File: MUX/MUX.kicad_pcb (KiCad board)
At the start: 4 copper layers, 364 x 203 mm, 100 parts, among them P1 Conn_02x36_Top_Bottom, P2 DB9_Male, P3 DB9_Male, P4 DB9_Male, P5 DB9_Male

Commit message: MUX: Start of the layout
Let's see how it goes...
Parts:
- moved R16 24.6 mm to (290.8, 170.6)
- moved R15 4.19 mm to (321.3, 55.5)
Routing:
- net /~{Reset}: track 0.00 -> 268.7 mm, vias 0 -> 1
- net /Reset: track 0.00 -> 263.3 mm
- net /~{INT_Request}: track 0.00 -> 230.4 mm, vias 0 -> 1
- net /~{CommonAddressed}: track 0.00 -> 194.2 mm, vias 0 -> 2
- net /Data.InBD_{5}: track 0.00 -> 178.2 mm
- net /Data.InBD_{6}: track 0.00 -> 176.9 mm
- net /CausePending: track 0.00 -> 170.7 mm
- net /~{INT_INH}: track 0.00 -> 167.5 mm, vias 0 -> 1
- net /MUXClock: track 0.00 -> 159.4 mm
- net /LevelAllow: track 0.00 -> 154.9 mm
- net /INT_Request: track 0.00 -> 144.2 mm
- net Net-(U_A4-Pad1): track 0.00 -> 134.5 mm, vias 0 -> 1
- net Net-(R_C4RN1-Pad1): track 0.00 -> 128.3 mm
- net Net-(R_C4RN1-Pad2): track 0.00 -> 122.7 mm
- net Net-(R_C4RN1-Pad3): track 0.00 -> 121.7 mm
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
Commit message: MUX: Place capacitors and some power layout
Place decoupling capacitors and do some power layout to try it out
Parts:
- added C1: 100nF, Capacitor_THT:C_Disc_D4.3mm_W1.9mm_P5.00mm, F.Cu at (80.4, 46.6)
- added C10: 1000uF, Capacitor_THT:CP_Radial_D8.0mm_P3.50mm, F.Cu at (174.9, 215.9)
- added C11: 100nF, Capacitor_THT:C_Disc_D4.3mm_W1.9mm_P5.00mm, F.Cu at (209.4, 46.4)
- added C12: 100nF, Capacitor_THT:C_Disc_D4.3mm_W1.9mm_P5.00mm, F.Cu at (209.0, 69.4)
- added C13: 100nF, Capacitor_THT:C_Disc_D4.3mm_W1.9mm_P5.00mm, F.Cu at (208.8, 92.5)
- added C14: 100nF, Capacitor_THT:C_Disc_D4.3mm_W1.9mm_P5.00mm, F.Cu at (206.4, 116.3)
- added C15: 100nF, Capacitor_THT:C_Disc_D4.3mm_W1.9mm_P5.00mm, F.Cu at (208.3, 139.3)
- added C16: 100nF, Capacitor_THT:C_Disc_D4.3mm_W1.9mm_P5.00mm, F.Cu at (209.7, 162.6)
- added C17: 100nF, Capacitor_THT:C_Disc_D4.3mm_W1.9mm_P5.00mm, F.Cu at (209.4, 186.8)
- added C18: 100nF, Capacitor_THT:C_Disc_D4.3mm_W1.9mm_P5.00mm, F.Cu at (209.4, 209.9)
- added C2: 100nF, Capacitor_THT:C_Disc_D4.3mm_W1.9mm_P5.00mm, F.Cu at (80.0, 69.8)
- added C20: 1000uF, Capacitor_THT:CP_Radial_D8.0mm_P3.50mm, F.Cu at (364.6, 40.6)
- added C21: 100nF, Capacitor_THT:C_Disc_D4.3mm_W1.9mm_P5.00mm, F.Cu at (334.0, 46.9)
- added C22: 100nF, Capacitor_THT:C_Disc_D4.3mm_W1.9mm_P5.00mm, F.Cu at (334.0, 70.2)
- added C23: 100nF, Capacitor_THT:C_Disc_D4.3mm_W1.9mm_P5.00mm, F.Cu at (335.0, 93.3)
- added C24: 100nF, Capacitor_THT:C_Disc_D4.3mm_W1.9mm_P5.00mm, F.Cu at (332.2, 116.8)
- added C25: 100nF, Capacitor_THT:C_Disc_D4.3mm_W1.9mm_P5.00mm, F.Cu at (334.0, 139.8)
- added C26: 100nF, Capacitor_THT:C_Disc_D4.3mm_W1.9mm_P5.00mm, F.Cu at (332.6, 163.8)
- added C27: 100nF, Capacitor_THT:C_Disc_D4.3mm_W1.9mm_P5.00mm, F.Cu at (332.6, 186.3)
- added C28: 100nF, Capacitor_THT:C_Disc_D4.3mm_W1.9mm_P5.00mm, F.Cu at (333.9, 209.5)
- added C29: 1000uF, Capacitor_THT:CP_Radial_D8.0mm_P3.50mm, F.Cu at (364.6, 208.7)
- added C3: 100nF, Capacitor_THT:C_Disc_D4.3mm_W1.9mm_P5.00mm, F.Cu at (80.0, 88.4)
- added C31: 100nF, Capacitor_THT:C_Disc_D4.3mm_W1.9mm_P5.00mm, F.Cu at (64.8, 215.2)
- added C32: 100nF, Capacitor_THT:C_Disc_D4.3mm_W1.9mm_P5.00mm, F.Cu at (113.0, 186.3)
- added C33: 100nF, Capacitor_THT:C_Disc_D4.3mm_W1.9mm_P5.00mm, F.Cu at (176.5, 47.2)
- added C34: 100nF, Capacitor_THT:C_Disc_D4.3mm_W1.9mm_P5.00mm, F.Cu at (176.5, 116.5)
- added C35: 100nF, Capacitor_THT:C_Disc_D4.3mm_W1.9mm_P5.00mm, F.Cu at (40.0, 126.4)
- added C36: 100nF, Capacitor_THT:C_Disc_D4.3mm_W1.9mm_P5.00mm, F.Cu at (38.6, 163.4)
- added C4: 100nF, Capacitor_THT:C_Disc_D4.3mm_W1.9mm_P5.00mm, F.Cu at (80.3, 116.3)
- added C5: 100nF, Capacitor_THT:C_Disc_D4.3mm_W1.9mm_P5.00mm, F.Cu at (80.1, 139.5)
- added C6: 100nF, Capacitor_THT:C_Disc_D4.3mm_W1.9mm_P5.00mm, F.Cu at (79.9, 163.2)
- added C7: 100nF, Capacitor_THT:C_Disc_D4.3mm_W1.9mm_P5.00mm, F.Cu at (80.1, 186.1)
- added C8: 1000uF, Capacitor_THT:CP_Radial_D8.0mm_P3.50mm, F.Cu at (98.8, 33.4)
- added C9: 100nF, Capacitor_THT:C_Disc_D4.3mm_W1.9mm_P5.00mm, F.Cu at (113.0, 209.5)
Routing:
- net GND: track 41.7 -> 883.2 mm
- net +5V: track 100.3 -> 683.3 mm, vias 0 -> 1
- net +12V: track 0.00 -> 315.2 mm, vias 0 -> 1
- net -12V: track 0.00 -> 253.2 mm, vias 0 -> 2
- net /DirectAddressed: track 17.6 -> 43.8 mm
- net /SysA_{0}: track 120.1 -> 128.4 mm
- net /SysA_{1}: track 120.0 -> 128.0 mm
- net Net-(U_A4-Pad9): track 101.1 -> 108.5 mm
- net /~{Reset}: track 268.7 -> 261.5 mm, vias 1 -> 2
- net /INR_OUT: track 104.7 -> 99.7 mm
- net /SysA_{2}: track 112.1 -> 107.7 mm
- net Sys.~{RDIN}: track 83.4 -> 79.6 mm
- net Net-(U_A4-Pad1): track 134.5 -> 138.2 mm
- net /LevelAllow: track 154.9 -> 158.3 mm
- net /SysA_{3}: track 109.6 -> 112.9 mm
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
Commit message: MUX layout
Work in progress
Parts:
- moved R16 4.44 mm to (290.8, 175.0)
- moved C17 0.51 mm to (209.5, 186.3)
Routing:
- net +5V: track 683.3 -> 1164.4 mm
- net /Phase1: track 0.00 -> 315.3 mm
- net /~{CommonRead}: track 69.0 -> 286.8 mm
- net /~{DirectRead}: track 0.00 -> 180.5 mm, vias 0 -> 2
- net /Data.OutD_{7}: track 88.1 -> 258.3 mm, vias 0 -> 1
- net /ForceTXEInt: track 0.00 -> 168.0 mm, vias 0 -> 1
- net /~{StatusOut}: track 53.5 -> 216.2 mm, vias 0 -> 2
- net /Data.InBD_{1}: track 37.8 -> 197.4 mm
- net /Phase3: track 0.00 -> 153.2 mm, vias 0 -> 1
- net /Data.InBD_{0}: track 46.2 -> 193.7 mm
- net Net-(U_C7-Pad1): track 0.00 -> 145.6 mm, vias 0 -> 1
- net /Data.OutD_{5}: track 93.1 -> 232.1 mm, vias 0 -> 2
- net /Data.OutD_{0}: track 75.2 -> 197.0 mm, vias 0 -> 2
- net Net-(U_D5-Pad2): track 0.00 -> 115.7 mm
- net /~{DirectAddressed}: track 53.5 -> 163.7 mm, vias 0 -> 1
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
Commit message: MUX: More layout
4 rows done
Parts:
- moved TP1 16.6 mm to (140.2, 190.6)
- moved C33 7.16 mm to (176.5, 40.0)
- moved C13 1.11 mm to (209.5, 93.4)
- moved C14 0.51 mm to (206.4, 116.8)
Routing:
- net GND: track 935.8 -> 1593.5 mm, vias 0 -> 1
- net +5V: track 1164.4 -> 1492.9 mm
- net /LoadCR_{0}: track 0.00 -> 258.3 mm, vias 0 -> 3
- net /Data.OutD_{2}: track 137.4 -> 371.3 mm, vias 1 -> 2
- net /Data.OutD_{4}: track 151.4 -> 384.1 mm
- net /Data.OutD_{1}: track 118.0 -> 340.5 mm, vias 1 -> 3
- net /Data.OutD_{3}: track 137.1 -> 356.1 mm, vias 1 -> 4
- net /Data.InBD_{4}: track 0.00 -> 209.3 mm, vias 0 -> 1
- net /Data.InBD_{2}: track 119.3 -> 301.8 mm, vias 0 -> 2
- net /Data.InBD_{7}: track 0.00 -> 177.4 mm, vias 0 -> 1
- net /~{Reset}: track 262.6 -> 437.8 mm
- net /Data.OutD_{5}: track 232.1 -> 402.4 mm, vias 2 -> 3
- net /TxBE_{0}: track 0.00 -> 164.9 mm, vias 0 -> 3
- net /~{LoadTxB_{0}}: track 0.00 -> 159.6 mm, vias 0 -> 1
- net /Data.OutD_{0}: track 197.0 -> 356.0 mm, vias 2 -> 3
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
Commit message: MUX: Routing
6 rows done
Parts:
- moved C34 3.46 mm to (173.1, 116.6)
- moved C4 0.57 mm to (80.0, 116.8)
- moved C1 0.54 mm to (80.0, 46.9)
- moved C14 0.53 mm to (206.9, 116.8)
- moved C18 0.39 mm to (209.4, 209.5)
- moved C2 0.35 mm to (80.0, 70.2)
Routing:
- net +5V: track 1492.9 -> 2321.0 mm, vias 1 -> 0
- net GND: track 1593.5 -> 2079.3 mm, vias 1 -> 2
- net /LoadCR_{1}: track 0.00 -> 235.7 mm, vias 0 -> 1
- net /Data.InBD_{5}: track 268.1 -> 481.2 mm, vias 1 -> 2
- net /LoadCR_{2}: track 0.00 -> 208.3 mm, vias 0 -> 1
- net /Data.InBD_{6}: track 263.4 -> 471.5 mm, vias 1 -> 2
- net /Data.InBD_{7}: track 177.4 -> 384.4 mm, vias 1 -> 2
- net /Data.InBD_{0}: track 313.7 -> 512.8 mm
- net /LoadCR_{3}: track 0.00 -> 198.2 mm, vias 0 -> 1
- net /CTS_{1}_TTL: track 0.00 -> 177.5 mm, vias 0 -> 2
- net Net-(U_F5-Pad1): track 0.00 -> 170.4 mm
- net /CTS_{0}_TTL: track 0.00 -> 168.5 mm, vias 0 -> 2
- net Net-(U_F5-Pad12): track 0.00 -> 152.7 mm, vias 0 -> 1
- net /Data.InBD_{2}: track 301.8 -> 439.5 mm
- net /Data.InBD_{1}: track 311.2 -> 444.2 mm
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
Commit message: MUX: More layout
8 columns done
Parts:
- moved C10 193.3 mm to (368.1, 210.1), turned to 180 degrees
- moved R20 31.1 mm to (146.7, 179.9), turned to 180 degrees
- moved R13 27.3 mm to (168.9, 214.4), turned to 180 degrees
- moved C31 19.3 mm to (60.1, 196.5), turned to 180 degrees
- moved C29 11.0 mm to (364.5, 197.6)
- moved R21 10.2 mm to (146.7, 187.7), turned to 180 degrees
- moved C16 3.80 mm to (206.5, 160.6), turned to 0 degrees
- moved C33 2.23 mm to (175.3, 41.9)
- moved TP1 1.34 mm to (139.0, 191.2)
- moved C11 0.69 mm to (208.7, 46.5)
- moved C14 0.20 mm to (207.1, 116.8)
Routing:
- net +5V: track 2321.0 -> 3205.2 mm, vias 0 -> 1
- net GND: track 2079.3 -> 2453.2 mm, vias 2 -> 4
- net Net-(U_H7-Pad15): track 0.00 -> 179.6 mm, vias 0 -> 2
- net /MUXClock: track 189.0 -> 346.3 mm
- net -12V: track 253.2 -> 398.5 mm
- net /~{TX_{3}_EIA}: track 7.62 -> 145.8 mm
- net Net-(U_K1-Pad1): track 0.00 -> 130.9 mm
- net /TX_{2}_OUT: track 0.00 -> 103.7 mm, vias 0 -> 1
- net /Data.InBD_{1}: track 444.2 -> 543.9 mm, vias 0 -> 1
- net /~{LoadCBR}: track 116.3 -> 214.2 mm, vias 1 -> 2
- net Net-(U_J6-Pad1): track 0.00 -> 96.8 mm
- net /Data.InBD_{2}: track 439.5 -> 534.9 mm, vias 2 -> 3
- net Net-(U_H7-Pad9): track 26.3 -> 118.9 mm, vias 0 -> 1
- net Net-(U_J7-Pad6): track 0.00 -> 84.6 mm, vias 0 -> 1
- net Net-(U_J6-Pad13): track 0.00 -> 83.8 mm
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
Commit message: MUX: Update the layout
Apply schematic corrections
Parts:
- U_K5: footprint Package_DIP:DIP-16_W7.62mm -> Package_DIP:DIP-14_W7.62mm
- moved C4 7.76 mm to (80.1, 124.6)
- moved C3 5.00 mm to (80.0, 93.4), turned to 90 degrees
- moved C8 2.54 mm to (98.1, 31.0), turned to -90 degrees
- moved C36 1.36 mm to (40.0, 163.4)
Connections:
- C31 pad 2: Net-(C31-Pad2) -> -12V
- C35 pad 2: Net-(C31-Pad2) -> -12V
- C36 pad 2: Net-(C31-Pad2) -> -12V
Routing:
- net GND: track 2453.2 -> 2889.2 mm
- net /RX_{0}_IN: track 0.00 -> 161.7 mm
- net /RX_{2}_IN: track 0.00 -> 159.9 mm, vias 0 -> 1
- net /RX_{3}_IN: track 0.00 -> 142.9 mm, vias 0 -> 1
- net /RX_{1}_IN: track 0.00 -> 142.1 mm, vias 0 -> 1
- net +5V: track 3205.2 -> 3323.7 mm
- net Net-(R6-Pad2): track 0.00 -> 96.2 mm
- net /MUXClock: track 346.3 -> 442.5 mm
- net Net-(U_K1-Pad13): track 52.6 -> 115.1 mm
- net Net-(U_K6-Pad1): track 0.00 -> 56.6 mm, vias 0 -> 1
- net /TX_{0}_TTL: track 0.00 -> 52.5 mm
- net /TX_{1}_TTL: track 0.00 -> 50.1 mm
- net Net-(U_K1-Pad2): track 50.5 -> 99.0 mm
- net Net-(U_K1-Pad3): track 51.6 -> 100.1 mm
- net Net-(U_H7-Pad15): track 179.6 -> 227.8 mm
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
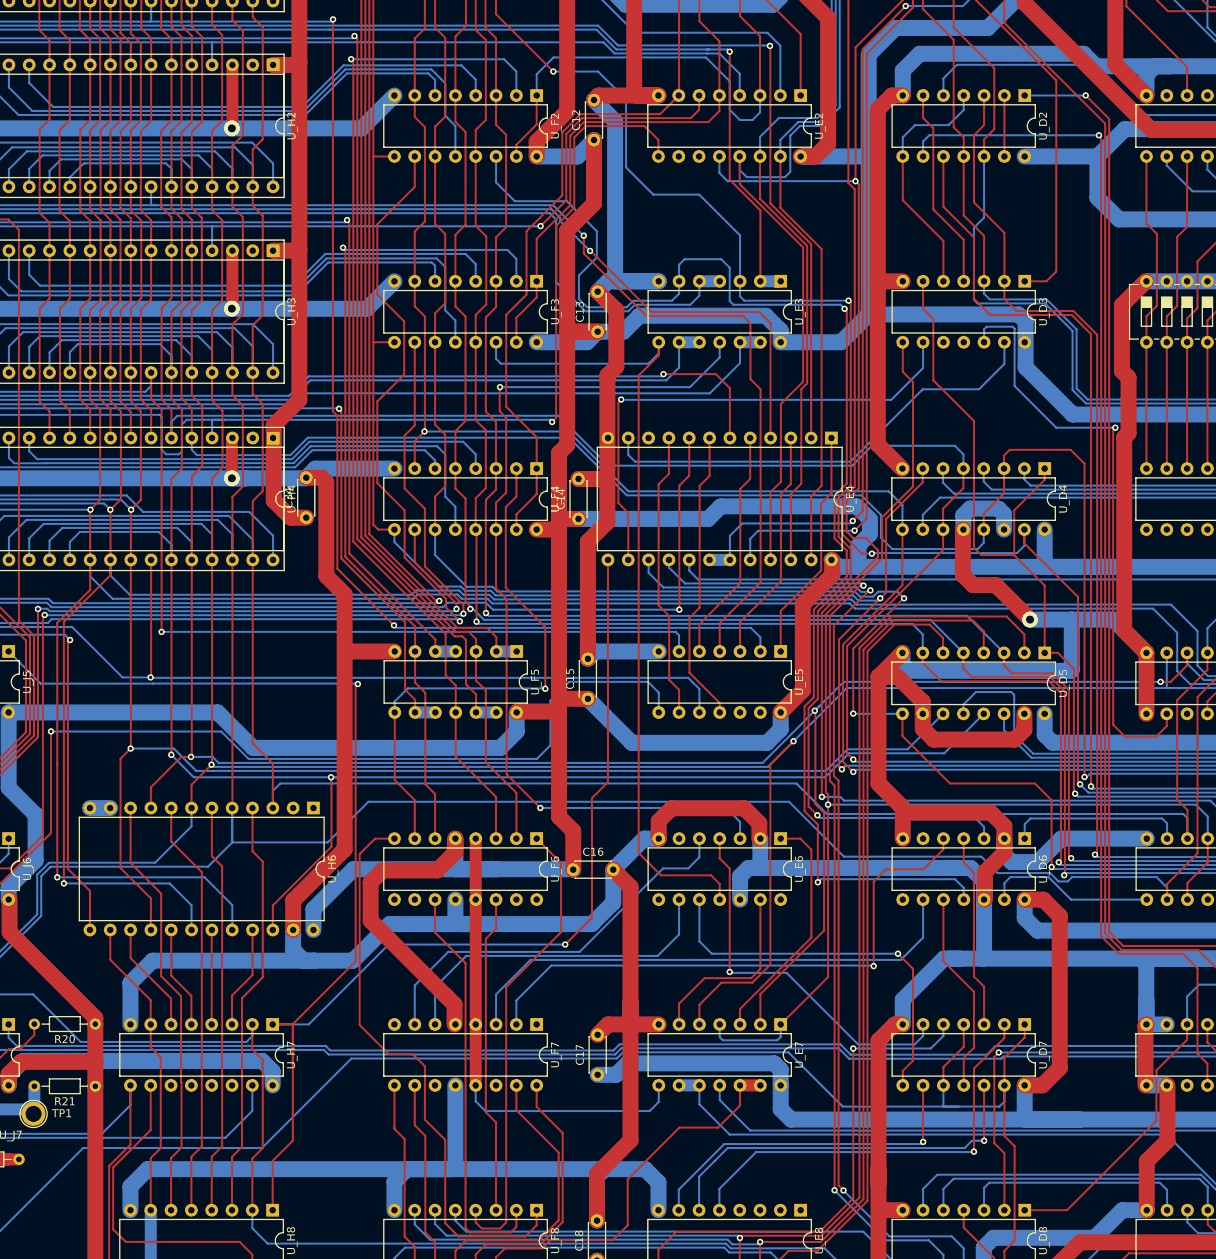
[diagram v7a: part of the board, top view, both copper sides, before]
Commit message: MUX: Avoid more unobtanium chips
- Replaced U_H6 with LS273
- Allow using russian К1533ИД3 as U_E4; it has narrow DIP package
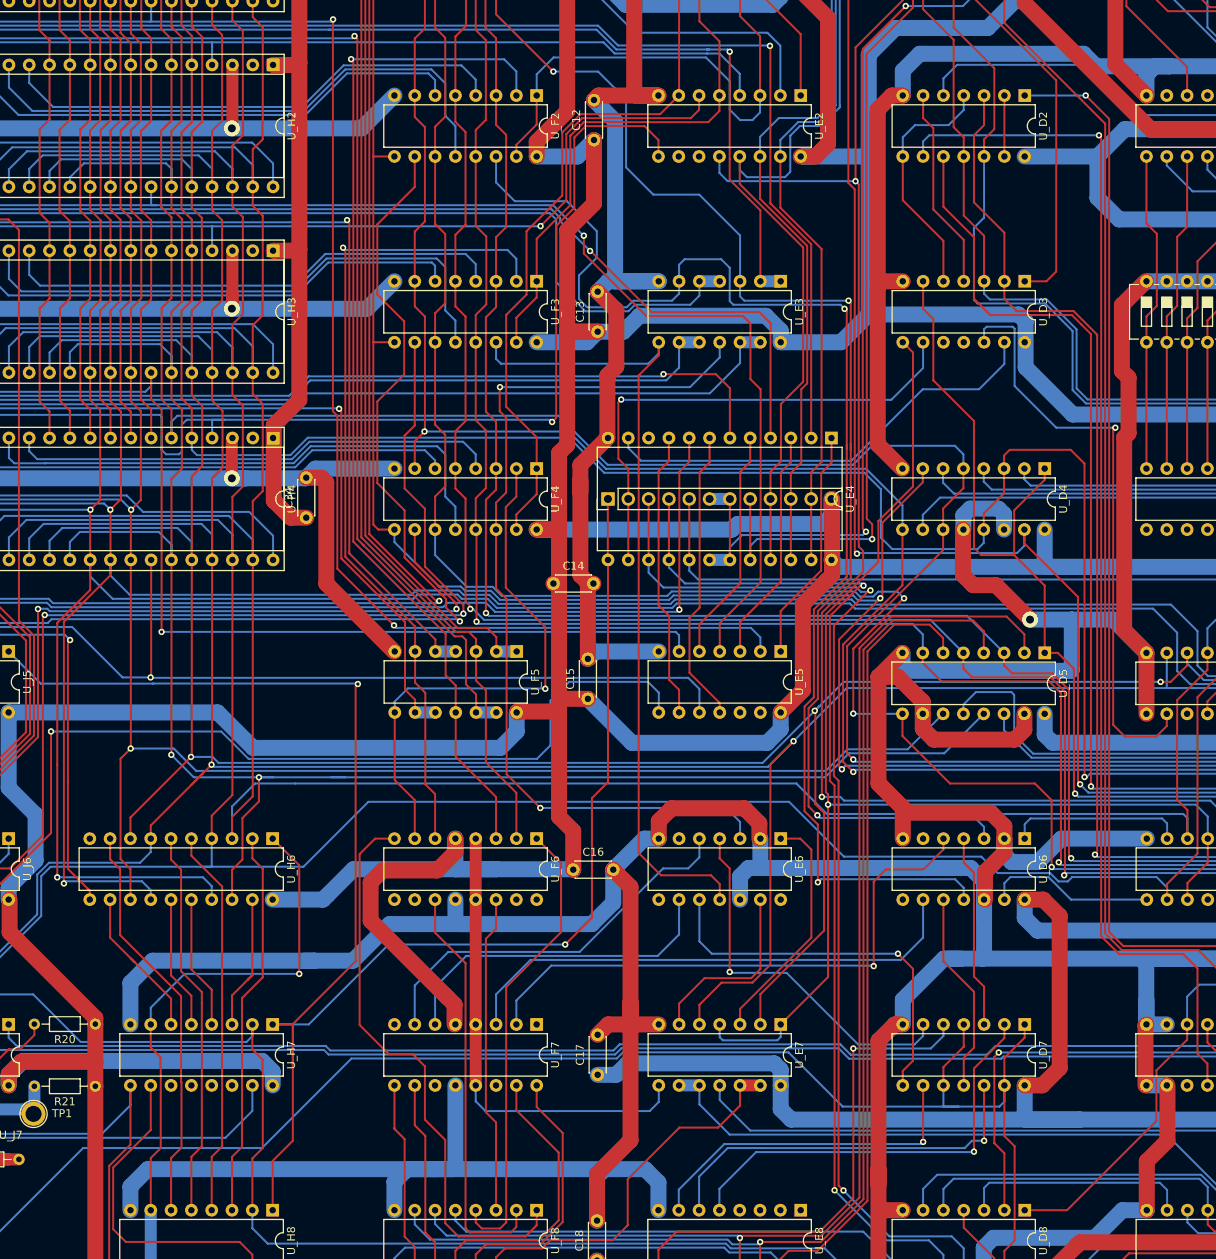
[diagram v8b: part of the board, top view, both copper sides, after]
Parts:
- added U_EB4: КР1533ИД3, Connector_PinHeader_2.54mm:PinHeader_1x12_P2.54mm_Vertical, F.Cu at (210.8, 114.3)
- U_H6: value SN74199 -> 74LS273; footprint Package_DIP:DIP-24_W15.24mm -> Package_DIP:DIP-20_W7.62mm
- moved C14 8.66 mm to (204.0, 124.9), turned to 0 degrees
- moved U_H6 6.38 mm to (168.9, 156.8)
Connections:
- R13 pad 2: Net-(R13-Pad2) -> Net-(U_H6-Pad1)
- U_H6 pad 1: unconnected-(U_H6-Pad1) -> Net-(U_H6-Pad1)
- U_H6 pad 10: Net-(U_H6-Pad10) -> GND
- U_H6 pad 11: GND -> Net-(U_J5-Pad2)
- U_H6 pad 12: GND -> Net-(U_H7-Pad6)
- U_H6 pad 13: Net-(U_H6-Pad13) -> /Data.InBD_{7}
- U_H6 pad 14: Net-(R13-Pad2) -> /Data.InBD_{6}
- U_H6 pad 15: Net-(U_H6-Pad15) -> Net-(U_H7-Pad5)
- U_H6 pad 16: /Data.InBD_{7} -> Net-(U_H7-Pad4)
- U_H6 pad 17: Net-(U_H6-Pad17) -> /Data.InBD_{5}
- U_H6 pad 18: /Data.InBD_{6} -> /Data.InBD_{4}
- U_H6 pad 19: Net-(U_H6-Pad19) -> Net-(U_H7-Pad3)
- U_H6 pad 2: unconnected-(U_H6-Pad2) -> Net-(U_H8-Pad3)
- U_H6 pad 20: /Data.InBD_{5} -> +5V
- U_H6 pad 4: Net-(U_H6-Pad4) -> /Data.InBD_{1}
- U_H6 pad 5: /Data.InBD_{1} -> Net-(U_H8-Pad4)
- U_H6 pad 6: Net-(U_H6-Pad6) -> Net-(U_H8-Pad5)
- U_H6 pad 8: Net-(U_H6-Pad8) -> /Data.InBD_{3}
- U_H6 pad 9: /Data.InBD_{3} -> Net-(U_H8-Pad6)
- U_H7 pad 3: Net-(U_H6-Pad21) -> Net-(U_H7-Pad3)
- U_H7 pad 4: Net-(U_H6-Pad19) -> Net-(U_H7-Pad4)
- U_H7 pad 5: Net-(U_H6-Pad17) -> Net-(U_H7-Pad5)
- U_H7 pad 6: Net-(U_H6-Pad15) -> Net-(U_H7-Pad6)
- U_H7 pad 7: Net-(R13-Pad2) -> Net-(U_H6-Pad1)
- U_H8 pad 10: Net-(R13-Pad2) -> Net-(U_H6-Pad1)
- U_H8 pad 3: Net-(U_H6-Pad4) -> Net-(U_H8-Pad3)
- U_H8 pad 4: Net-(U_H6-Pad6) -> Net-(U_H8-Pad4)
- U_H8 pad 5: Net-(U_H6-Pad8) -> Net-(U_H8-Pad5)
- U_H8 pad 6: Net-(U_H6-Pad10) -> Net-(U_H8-Pad6)
- U_H8 pad 7: Net-(R13-Pad2) -> Net-(U_H6-Pad1)
- U_J5 pad 2: Net-(U_H6-Pad13) -> Net-(U_J5-Pad2)
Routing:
- net Net-(U_H6-Pad1): track 0.00 -> 83.1 mm, vias 0 -> 1
- net Net-(R13-Pad2): track 56.3 -> 0.00 mm
- net Net-(U_H6-Pad10): track 53.4 -> 0.00 mm
- net Net-(U_H6-Pad8): track 52.4 -> 0.00 mm
- net Net-(U_H6-Pad4): track 52.4 -> 0.00 mm
- net Net-(U_H6-Pad6): track 51.3 -> 0.00 mm
- net Net-(U_H8-Pad6): track 0.00 -> 50.7 mm
- net Net-(U_H6-Pad13): track 49.7 -> 0.00 mm, vias 1 -> 0
- net GND: track 2889.2 -> 2840.1 mm
- net Net-(U_H8-Pad4): track 0.00 -> 48.6 mm
- net Net-(U_H8-Pad5): track 0.00 -> 48.6 mm
- net Net-(U_H8-Pad3): track 0.00 -> 48.6 mm
- net Net-(U_J5-Pad2): track 0.00 -> 46.3 mm, vias 0 -> 1
- net Net-(U_H7-Pad6): track 0.00 -> 19.5 mm
- net Net-(U_H7-Pad3): track 0.00 -> 17.4 mm
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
